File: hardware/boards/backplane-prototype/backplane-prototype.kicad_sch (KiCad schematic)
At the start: 32 parts, among them J1 SLOT_1, J2 i2c_backpack, J3 SLOT_2, J4 SLOT_3, J5 DC_IN, J6 SLOT_4, J7 SLOT_5, J8 SLOT_6

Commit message: Fix backplane production metadata
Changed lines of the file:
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@@
+	)
+	(symbol
+		(lib_id "power:PWR_FLAG")
+		(at 52.07 120.65 0)
+		(unit 1)
+		(body_style 1)
+		(exclude_from_sim no)
+		(in_bom yes)
+		(on_board yes)
+		(in_pos_files yes)
+		(dnp no)
+		(property "Reference" "#FLG02"
+			(at 52.07 127 0)
+			(hide yes)
+			(show_name no)
+			(do_not_autoplace no)
+			(effects
+				(font
+					(size 1.27 1.27)
+				)
+			)
+		)
+		(property "Value" "PWR_FLAG"
+			(at 52.578 115.316 0)
+			(hide yes)
+			(show_name no)
+			(do_not_autoplace no)
+			(effects
+				(font
+					(size 1.27 1.27)
+				)
+			)
+		)
+		(property "Footprint" ""
+			(at 52.07 120.65 0)
+			(hide yes)
+			(show_name no)
+			(do_not_autoplace no)
+			(effects
+				(font
+					(size 1.27 1.27)
+				)
+			)
+		)
+		(property "Datasheet" ""
+			(at 52.07 120.65 0)
+			(hide yes)
+			(show_name no)
+			(do_not_autoplace no)
+			(effects
+				(font
+					(size 1.27 1.27)
+				)
+			)
+		)
+		(property "Description" "Special symbol for telling ERC where power comes from"
+			(at 52.07 120.65 0)
+			(hide yes)
+			(show_name no)
+			(do_not_autoplace no)
+			(effects
+				(font
+					(size 1.27 1.27)
+				)
+			)
+		)
+		(pin "1"
+		)
+		(instances
+			(project "backplane-prototype"
+				(path "/348cc909-6345-4013-9bef-98714057a65b"
+					(reference "#FLG02")
+					(unit 1)
+				)
+			)
+		)
 	)
 	(symbol

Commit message: Add JLCPCB tooling-hole definitions
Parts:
- added H7, H8, H9: ToolingHole_1.152mm, mini-rack-power:MountingHole_JLCPCB_Tooling_1.152mm, symbol Mechanical:MountingHole
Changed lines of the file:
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@@
 		(in_bom no)
 		(on_board yes)
-		(in_pos_files yes)
+		(in_pos_files no)
 		(dnp no)
 		(fields_autoplaced yes)
@@
 		(in_bom no)
 		(on_board yes)
-		(in_pos_files yes)
+		(in_pos_files no)
 		(dnp no)
 		(fields_autoplaced yes)
@@
 		(in_bom no)
 		(on_board yes)
-		(in_pos_files yes)
+		(in_pos_files no)
 		(dnp no)
 		(fields_autoplaced yes)
@@
 		(in_bom no)
 		(on_board yes)
-		(in_pos_files yes)
+		(in_pos_files no)
 		(dnp yes)
 		(fields_autoplaced yes)
@@
 		(in_bom no)
 		(on_board yes)
-		(in_pos_files yes)
+		(in_pos_files no)
 		(dnp no)
 		(fields_autoplaced yes)
@@
 		(in_bom no)
 		(on_board yes)
-		(in_pos_files yes)
+		(in_pos_files no)
 		(dnp no)
 		(fields_autoplaced yes)
@@
 					(unit 1)
 				)
+			)
+		)
+	)
+	(symbol
+		(lib_id "Mechanical:MountingHole")
+		(at 91.44 168.91 0)
+		(unit 1)
+		(body_style 1)
+		(exclude_from_sim no)
+		(in_bom no)
+		(on_board yes)
+		(in_pos_files no)
+		(dnp no)
+		(property "Reference" "H7"
+			(at 91.44 165.1 0)
+			(show_name no)
+			(do_not_autoplace no)
+			(effects
+				(font
+					(size 1.27 1.27)
+				)
+			)
+		)
+		(property "Value" "ToolingHole_1.152mm"
+			(at 91.44 172.085 0)
+			(hide yes)
+			(show_name no)
+			(do_not_autoplace no)
+			(effects
+				(font
+					(size 1.27 1.27)
+				)
+			)
+		)
+		(property "Footprint" "mini-rack-power:MountingHole_JLCPCB_Tooling_1.152mm"
+			(at 91.44 168.91 0)
+			(hide yes)
+			(show_name no)
+			(do_not_autoplace no)
+			(effects
+				(font
+					(size 1.27 1.27)
+				)
+			)
+		)
+		(property "Datasheet" "https://jlcpcb.com/help/article/how-to-add-tooling-holes-for-pcb-assembly-order"
+			(at 91.44 168.91 0)
+			(hide yes)
+			(show_name no)
+			(do_not_autoplace no)
+			(effects
+				(font
+					(size 1.27 1.27)
+				)
+			)
+		)
+		(property "Description" "JLCPCB PCBA tooling hole, 1.152 mm round NPTH with 0.148 mm solder-mask expansion"
+			(at 91.44 168.91 0)
+			(hide yes)
+			(show_name no)
+			(do_not_autoplace no)
+			(effects
+				(font
+					(size 1.27 1.27)
+				)
+			)
+		)
+		(instances
+			(project "backplane-prototype"
+				(path "/348cc909-6345-4013-9bef-98714057a65b"
+					(reference "H7")
+					(unit 1)
+				)
+			)
+		)
+	)
+	(symbol
+		(lib_id "Mechanical:MountingHole")
+		(at 101.6 168.91 0)
+		(unit 1)
+		(body_style 1)
+		(exclude_from_sim no)
+		(in_bom no)
+		(on_board yes)
+		(in_pos_files no)
+		(dnp no)
+		(property "Reference" "H8"
+			(at 101.6 165.1 0)
+			(show_name no)
+			(do_not_autoplace no)
+			(effects
+				(font
+					(size 1.27 1.27)
+				)
+			)
+		)
+		(property "Value" "ToolingHole_1.152mm"
+			(at 101.6 172.085 0)
+			(hide yes)
+			(show_name no)
+			(do_not_autoplace no)
+			(effects
+				(font
+					(size 1.27 1.27)
+				)
+			)
+		)
+		(property "Footprint" "mini-rack-power:MountingHole_JLCPCB_Tooling_1.152mm"
+			(at 101.6 168.91 0)
+			(hide yes)
+			(show_name no)
+			(do_not_autoplace no)
+			(effects
+				(font
+					(size 1.27 1.27)
+				)
+			)
+		)
+		(property "Datasheet" "https://jlcpcb.com/help/article/how-to-add-tooling-holes-for-pcb-assembly-order"
+			(at 101.6 168.91 0)
+			(hide yes)
+			(show_name no)
+			(do_not_autoplace no)
+			(effects
+				(font
+					(size 1.27 1.27)
+				)
+			)
+		)
+		(property "Description" "JLCPCB PCBA tooling hole, 1.152 mm round NPTH with 0.148 mm solder-mask expansion"
+			(at 101.6 168.91 0)
+			(hide yes)
+			(show_name no)
+			(do_not_autoplace no)
+			(effects
+				(font
+					(size 1.27 1.27)
+				)
+			)
+		)
+		(instances
+			(project "backplane-prototype"
+				(path "/348cc909-6345-4013-9bef-98714057a65b"
+					(reference "H8")
+					(unit 1)
+				)
+			)
+		)
+	)
+	(symbol
+		(lib_id "Mechanical:MountingHole")
+		(at 111.76 168.91 0)
+		(unit 1)
+		(body_style 1)
+		(exclude_from_sim no)
+		(in_bom no)
+		(on_board yes)
+		(in_pos_files no)
+		(dnp no)
+		(property "Reference" "H9"
+			(at 111.76 165.1 0)
+			(show_name no)
+			(do_not_autoplace no)
+			(effects
+				(font
+					(size 1.27 1.27)
+				)
+			)
+		)
+		(property "Value" "ToolingHole_1.152mm"
+			(at 111.76 172.085 0)
+			(hide yes)
+			(show_name no)
+			(do_not_autoplace no)
+			(effects
+				(font
+					(size 1.27 1.27)
+				)
+			)
+		)
+		(property "Footprint" "mini-rack-power:MountingHole_JLCPCB_Tooling_1.152mm"
+			(at 111.76 168.91 0)
+			(hide yes)
+			(show_name no)
+			(do_not_autoplace no)
+			(effects
+				(font
+					(size 1.27 1.27)
+				)
+			)
+		)
+		(property "Datasheet" "https://jlcpcb.com/help/article/how-to-add-tooling-holes-for-pcb-assembly-order"
+			(at 111.76 168.91 0)
+			(hide yes)
+			(show_name no)
+			(do_not_autoplace no)
+			(effects
+				(font
+					(size 1.27 1.27)
+				)
+			)
+		)
+		(property "Description" "JLCPCB PCBA tooling hole, 1.152 mm round NPTH with 0.148 mm solder-mask expansion"
+			(at 111.76 168.91 0)
+			(hide yes)
+			(show_name no)
+			(do_not_autoplace no)
+			(effects
+				(font
+					(size 1.27 1.27)
+				)
+			)
+		)
+		(instances
+			(project "backplane-prototype"
+				(path "/348cc909-6345-4013-9bef-98714057a65b"
+					(reference "H9")
+					(unit 1)
+				)

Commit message: Capture current backplane design and production files
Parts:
- removed H4: MountingHole_Pad, mini-rack-power:MountingHole_2.2mm_M2_Pad_Via_JLC, symbol Mechanical:MountingHole_Pad
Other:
- note added: "For SMT/A services, need at least three mount/holding holes."
- note added: "Marked as DNP so it's not exported in the BOM for JLC Assembly. These are hand-solder after the boards come back"
- moved on the sheet: H7, H8, H9

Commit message: pcb: remove H6 and refill copper zones
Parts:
- removed H6: MountingHole_Pad, mini-rack-power:MountingHole_2.2mm_M2_Pad_Via_JLC, symbol Mechanical:MountingHole_Pad
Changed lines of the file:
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@@
-	)
-	(symbol
-		(lib_id "Mechanical:MountingHole_Pad")
-		(at 157.48 182.88 0)
-		(unit 1)
-		(body_style 1)
-		(exclude_from_sim no)
-		(in_bom no)
-		(on_board yes)
-		(in_pos_files no)
-		(dnp no)
-		(fields_autoplaced yes)
-		(property "Reference" "H6"
-			(at 160.02 181.6099 0)
-			(show_name no)
-			(do_not_autoplace no)
-			(effects
-				(font
-					(size 1.27 1.27)
-				)
-				(justify left)
-			)
-		)
-		(property "Value" "MountingHole_Pad"
-			(at 160.02 185.42 0)
-			(hide yes)
-			(show_name no)
-			(do_not_autoplace no)
-			(effects
-				(font
-					(size 1.27 1.27)
-				)
-				(justify left)
-			)
-		)
-		(property "Footprint" "mini-rack-power:MountingHole_2.2mm_M2_Pad_Via_JLC"
-			(at 157.48 182.88 0)
-			(hide yes)
-			(show_name no)
-			(do_not_autoplace no)
-			(effects
-				(font
-					(size 1.27 1.27)
-				)
-			)
-		)
-		(property "Datasheet" ""
-			(at 157.48 182.88 0)
-			(hide yes)
-			(show_name no)
-			(do_not_autoplace no)
-			(effects
-				(font
-					(size 1.27 1.27)
-				)
-			)
-		)
-		(property "Description" "Grounded M3 mounting hole"
-			(at 157.48 182.88 0)
-			(hide yes)
-			(show_name no)
-			(do_not_autoplace no)
-			(effects
-				(font
-					(size 1.27 1.27)
-				)
-			)
-		)
-		(pin "1"
-		)
-		(instances
-			(project "backplane-prototype"
-				(path "/348cc909-6345-4013-9bef-98714057a65b"
-					(reference "H6")
-					(unit 1)
-				)
-			)
-		)
 	)
 	(symbol
@@
 					(unit 1)
 				)
-			)
-		)
-	)
-	(symbol
-		(lib_id "power:GND")
-		(at 157.48 185.42 0)
-		(unit 1)
-		(body_style 1)
-		(exclude_from_sim no)
-		(in_bom yes)
-		(on_board yes)
-		(in_pos_files yes)
-		(dnp no)
-		(fields_autoplaced yes)
-		(property "Reference" "#PWR016"
-			(at 157.48 191.77 0)
-			(hide yes)
-			(show_name no)
-			(do_not_autoplace no)
-			(effects
-				(font
-					(size 1.27 1.27)
-				)
-			)
-		)
-		(property "Value" "GND"
-			(at 157.48 190.5 0)
-			(show_name no)
-			(do_not_autoplace no)
-			(effects
-				(font
-					(size 1.27 1.27)
-				)
-			)
-		)
-		(property "Footprint" ""
-			(at 157.48 185.42 0)
-			(hide yes)
-			(show_name no)
-			(do_not_autoplace no)
-			(effects
-				(font
-					(size 1.27 1.27)
-				)
-			)
-		)
-		(property "Datasheet" ""
-			(at 157.48 185.42 0)
-			(hide yes)
-			(show_name no)
-			(do_not_autoplace no)
-			(effects
-				(font
-					(size 1.27 1.27)
-				)
-			)
-		)
-		(property "Description" "Power symbol creates a global label with name \"GND\" , ground"
-			(at 157.48 185.42 0)
-			(hide yes)
-			(show_name no)
-			(do_not_autoplace no)
-			(effects
-				(font
-					(size 1.27 1.27)
-				)
-			)
-		)
-		(pin "1"
-		)
-		(instances
-			(project "backplane-prototype"
-				(path "/348cc909-6345-4013-9bef-98714057a65b"
-					(reference "#PWR016")
-					(unit 1)
-				)

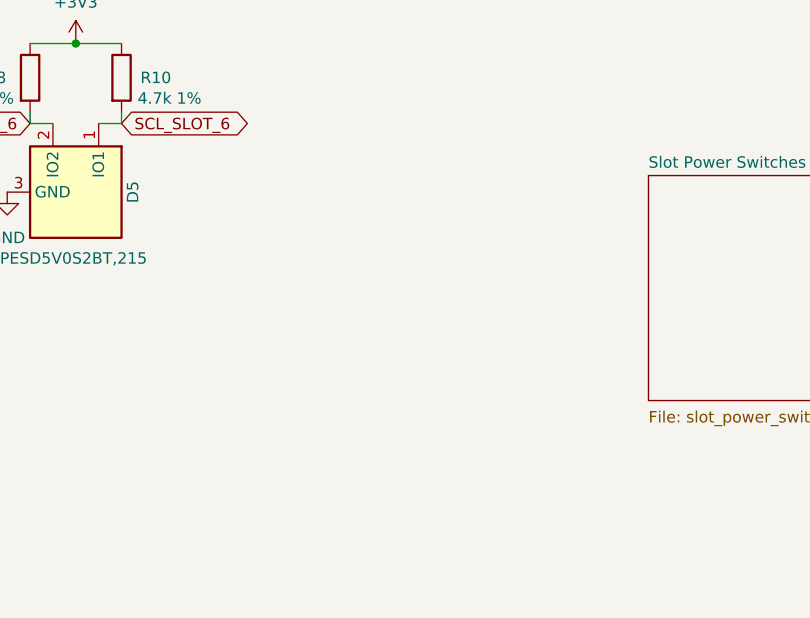
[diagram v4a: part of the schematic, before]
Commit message: hardware: add backplane temperature sensor
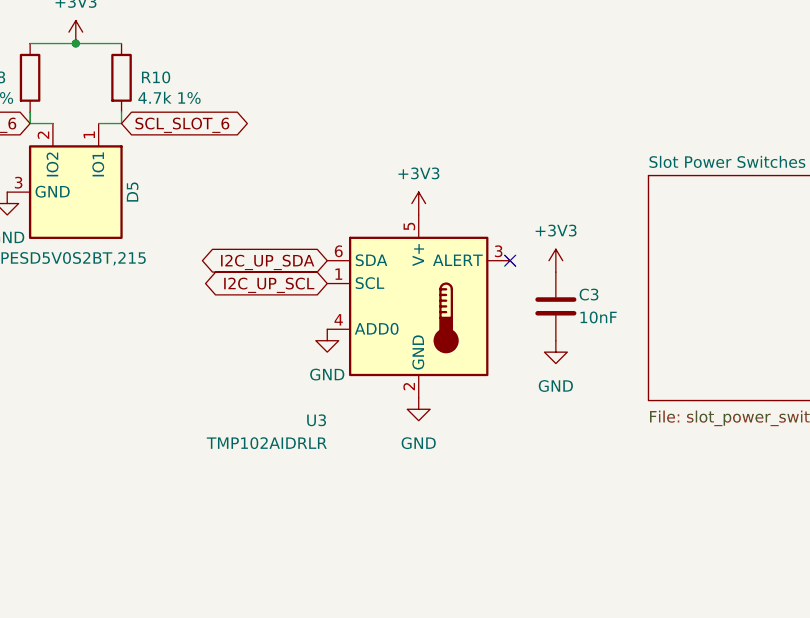
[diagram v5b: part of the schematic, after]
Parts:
- added C3: 10nF, Capacitor_SMD:C_0603_1608Metric, symbol Device:C
- added U3: TMP102AIDRLR, Package_TO_SOT_SMD:Texas_R-PDSO-N6_DRL-6, symbol Sensor_Temperature:TMP102xxDRL
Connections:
- net +3V3: now also C3.1, U3.5 (V+)
- net GND: now also C3.2, U3.2 (GND), U3.4 (ADD0)
- net I2C_UP_SCL: now also U3.1 (SCL)
- net I2C_UP_SDA: now also U3.6 (SDA)
- no-connect marks 0 -> 1

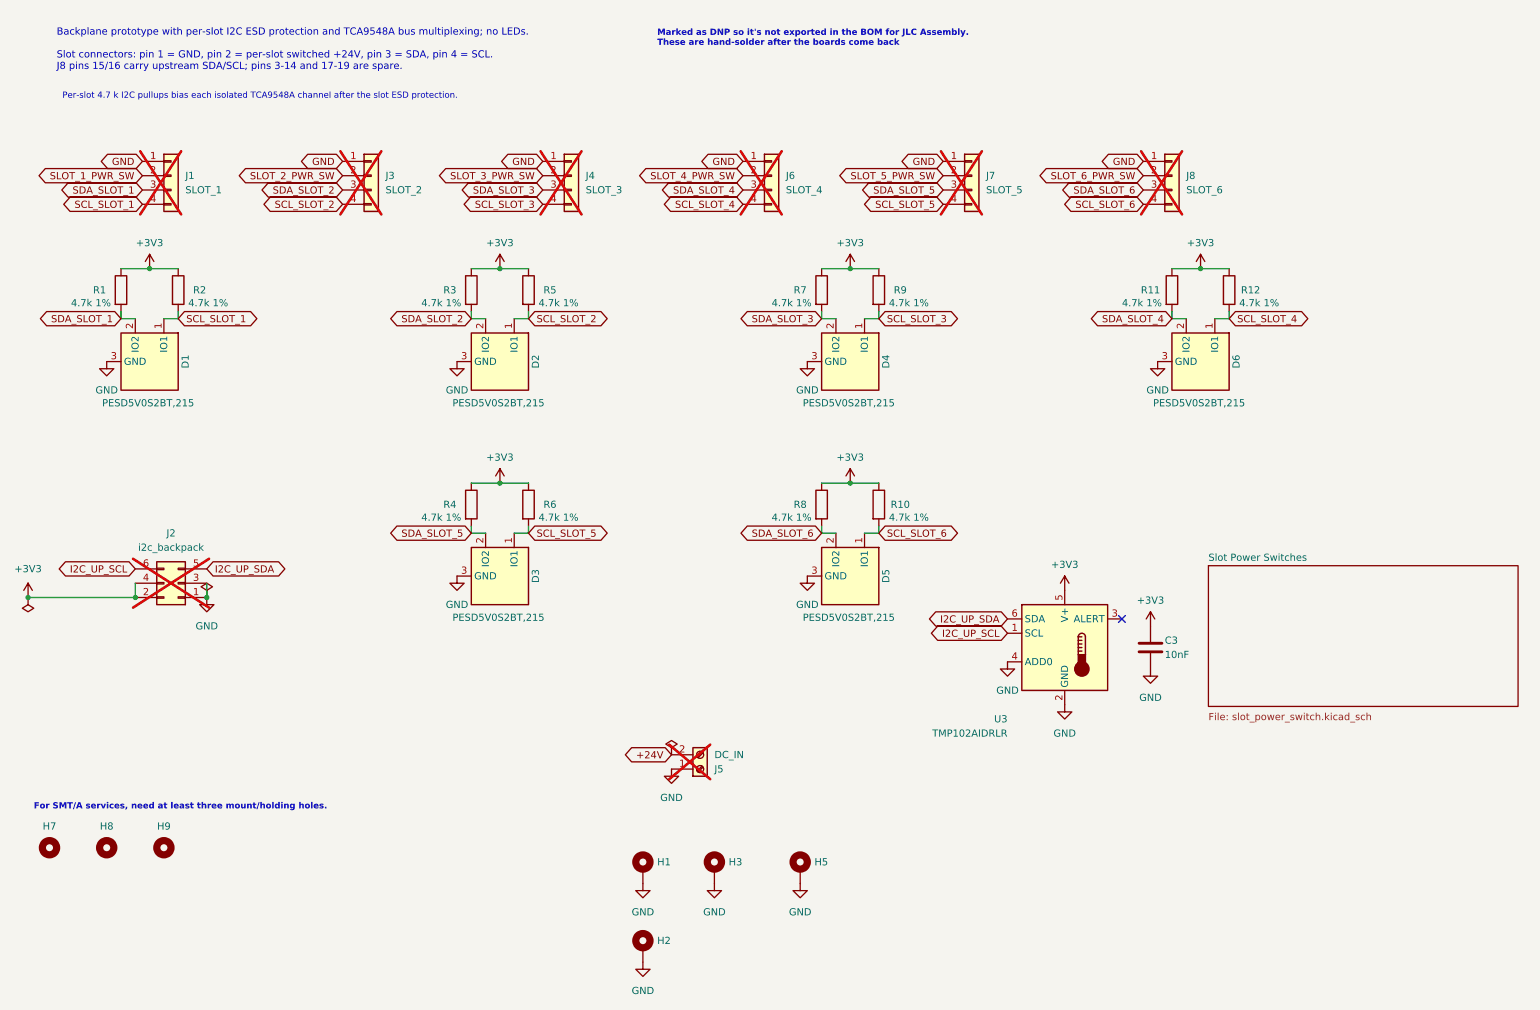
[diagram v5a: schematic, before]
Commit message: hardware: consolidate backplane schematic
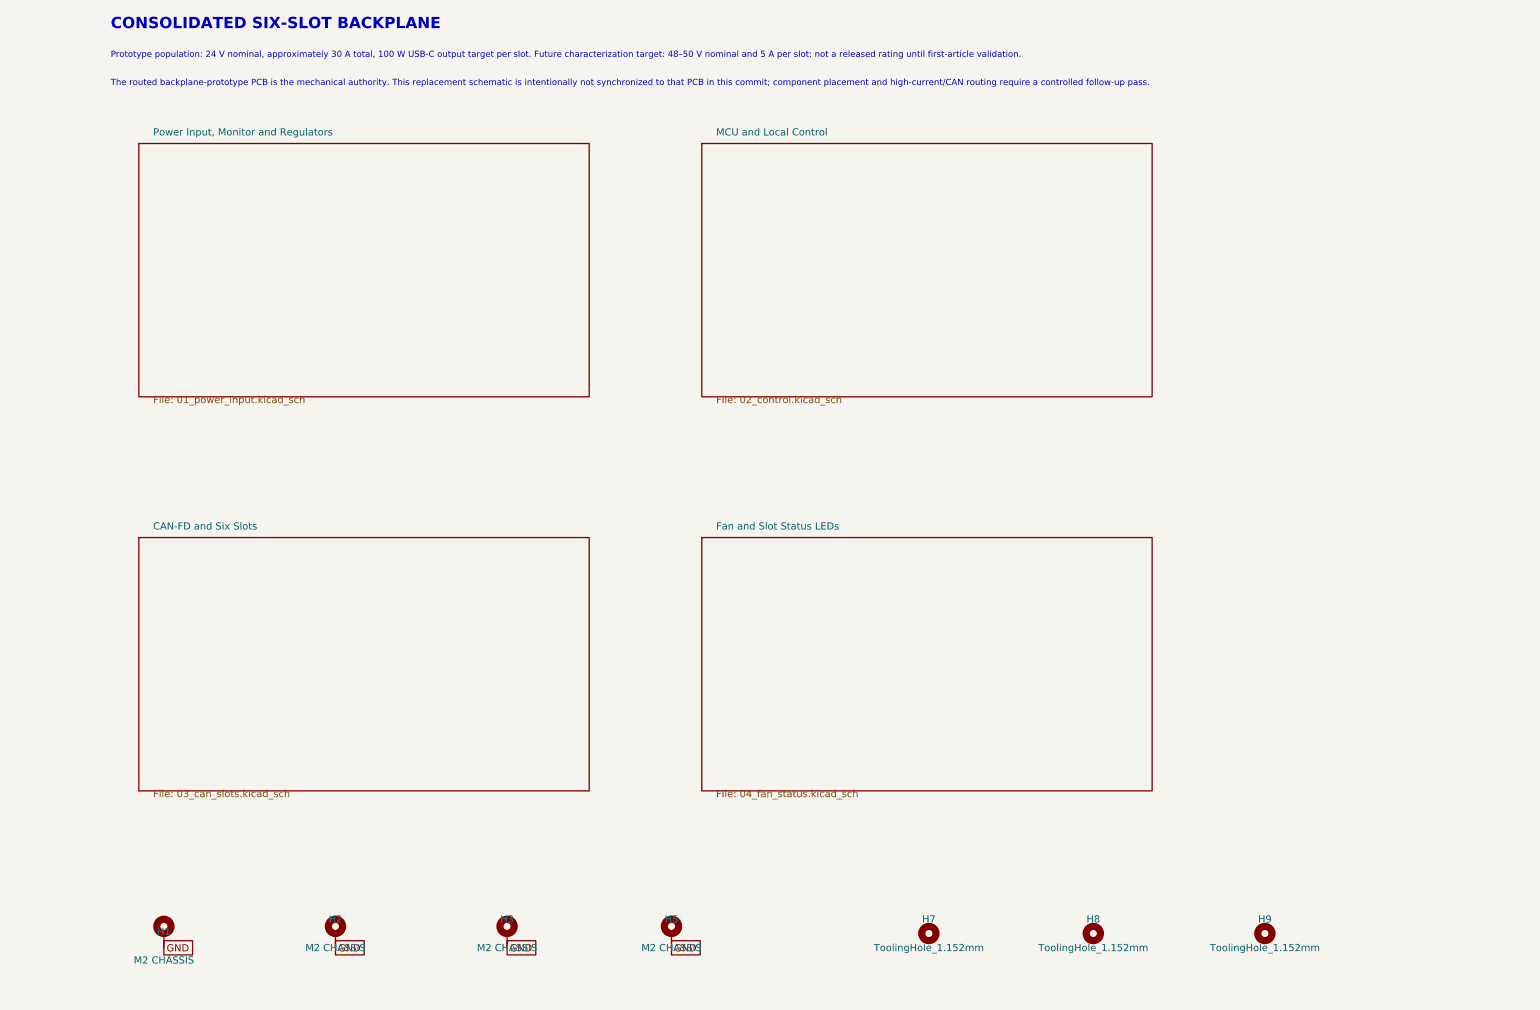
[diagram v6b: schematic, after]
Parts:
- removed C3: 10nF, Capacitor_SMD:C_0603_1608Metric, symbol Device:C
- removed D1, D2, D3, D4, D5, D6: PESD5V0S2BT,215, Package_TO_SOT_SMD:SOT-23, symbol backplane-backpack:PESD_Dual_SOT23
- removed J1: SLOT_1, mini-rack-power:Amass_XT30U_2plus2_F, symbol Connector_Generic:Conn_01x04
- removed J2: i2c_backpack, Connector_PinHeader_2.54mm:PinHeader_2x03_P2.54mm_Vertical, symbol Connector_Generic:Conn_02x03_Odd_Even
- removed J3: SLOT_2, mini-rack-power:Amass_XT30U_2plus2_F, symbol Connector_Generic:Conn_01x04
- removed J4: SLOT_3, mini-rack-power:Amass_XT30U_2plus2_F, symbol Connector_Generic:Conn_01x04
- removed J5: DC_IN, mini-rack-power:DORABO_DB910-6.35-2P-GN-S, symbol Connector:Screw_Terminal_01x02
- removed J6: SLOT_4, mini-rack-power:Amass_XT30U_2plus2_F, symbol Connector_Generic:Conn_01x04
- removed J7: SLOT_5, mini-rack-power:Amass_XT30U_2plus2_F, symbol Connector_Generic:Conn_01x04
- removed J8: SLOT_6, mini-rack-power:Amass_XT30U_2plus2_F, symbol Connector_Generic:Conn_01x04
- removed R1, R10, R11, R12, R2, R3, R4, R5, R6, R7, R8, R9: 4.7k 1%, Resistor_SMD:R_0603_1608Metric, symbol Device:R
- removed U3: TMP102AIDRLR, Package_TO_SOT_SMD:Texas_R-PDSO-N6_DRL-6, symbol Sensor_Temperature:TMP102xxDRL
- H1, H2, H3, H5: value MountingHole_Pad -> M2 CHASSIS; now in the parts list
- H7, H8, H9: now in the parts list
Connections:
- no-connect marks 1 -> 0
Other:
- removed sheet Slot Power Switches
- added sheet CAN-FD and Six Slots (03_can_slots.kicad_sch)
- added sheet Fan and Slot Status LEDs (04_fan_status.kicad_sch)
- added sheet MCU and Local Control (02_control.kicad_sch)
- added sheet Power Input, Monitor and Regulators (01_power_input.kicad_sch)
- note added: "CONSOLIDATED SIX-SLOT BACKPLANE"
- note added: "Prototype population: 24 V nominal, approximately 30 A total, 100 W USB-C output target per slot. Future characterization target: 48–50 V nominal and 5 A per slot; not a released rating until first-article validation."
- note added: "The routed backplane-prototype PCB is the mechanical authority. This replacement schematic is intentionally not synchronized to that PCB in this commit; component placement and high-current/CAN routing require a controlled follow-up pass."
- note removed: "Backplane prototype with per-slot I2C ESD protection and TCA9548A bus multiplexing; no LEDs."
- note removed: "For SMT/A services, need at least three mount/holding holes."
- note removed: "Marked as DNP so it's not exported in the BOM for JLC Assembly. These are hand-solder after the boards come back"
- note removed: "Per-slot 4.7 k I2C pullups bias each isolated TCA9548A channel after the slot ESD protection."
- note removed: "Slot connectors: pin 1 = GND, pin 2 = per-slot switched +24V, pin 3 = SDA, pin 4 = SCL. J8 pins 15/16 carry upstream SDA/SCL; pins 3-14 and 17-19 are spare."
- title: Backplane Prototype -> (none)
